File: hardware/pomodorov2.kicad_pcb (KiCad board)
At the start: 2 copper layers, 56 x 41.4 mm, 26 parts, among them J1 USB_B_Micro, J2 TC2050-IDC, J3 SOICbite, U1 MDBT50Q-1MV2, Y1 32.768kHz, Y1 32MHz, Y2 32.768kHz

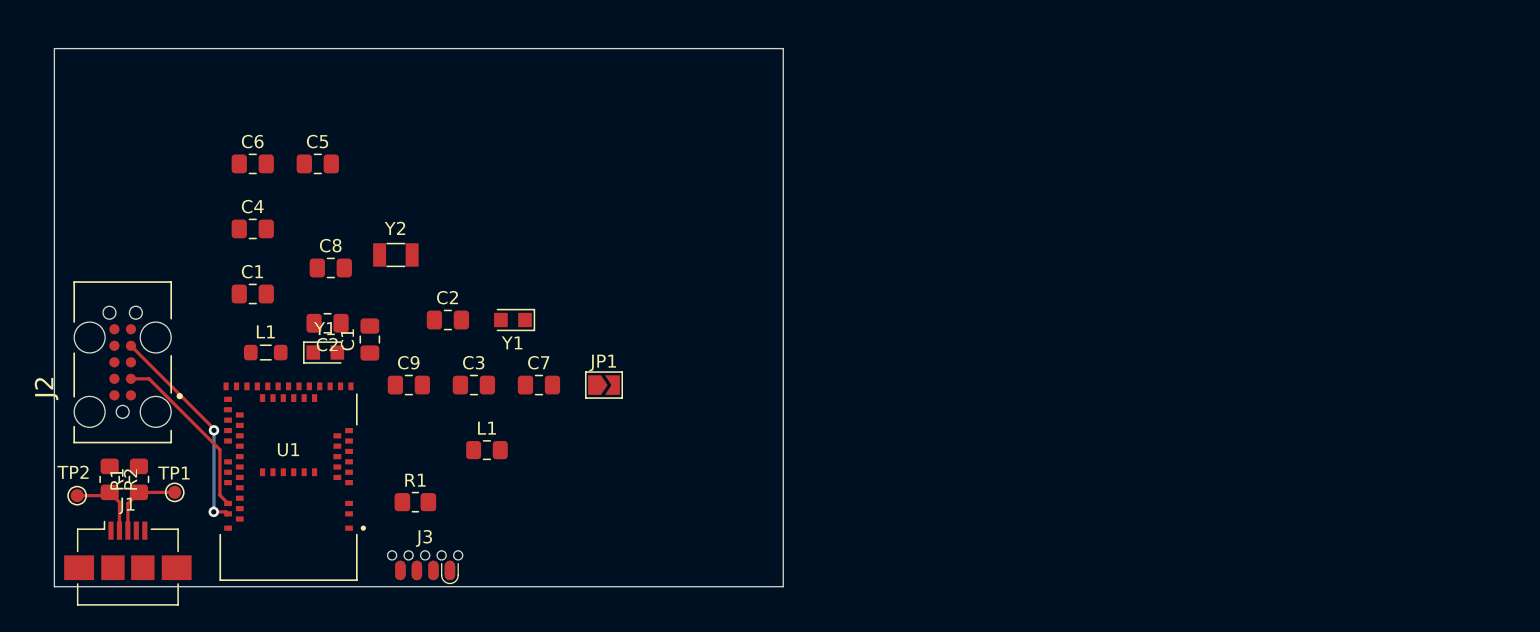
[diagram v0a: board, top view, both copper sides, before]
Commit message: Start on triangular layout
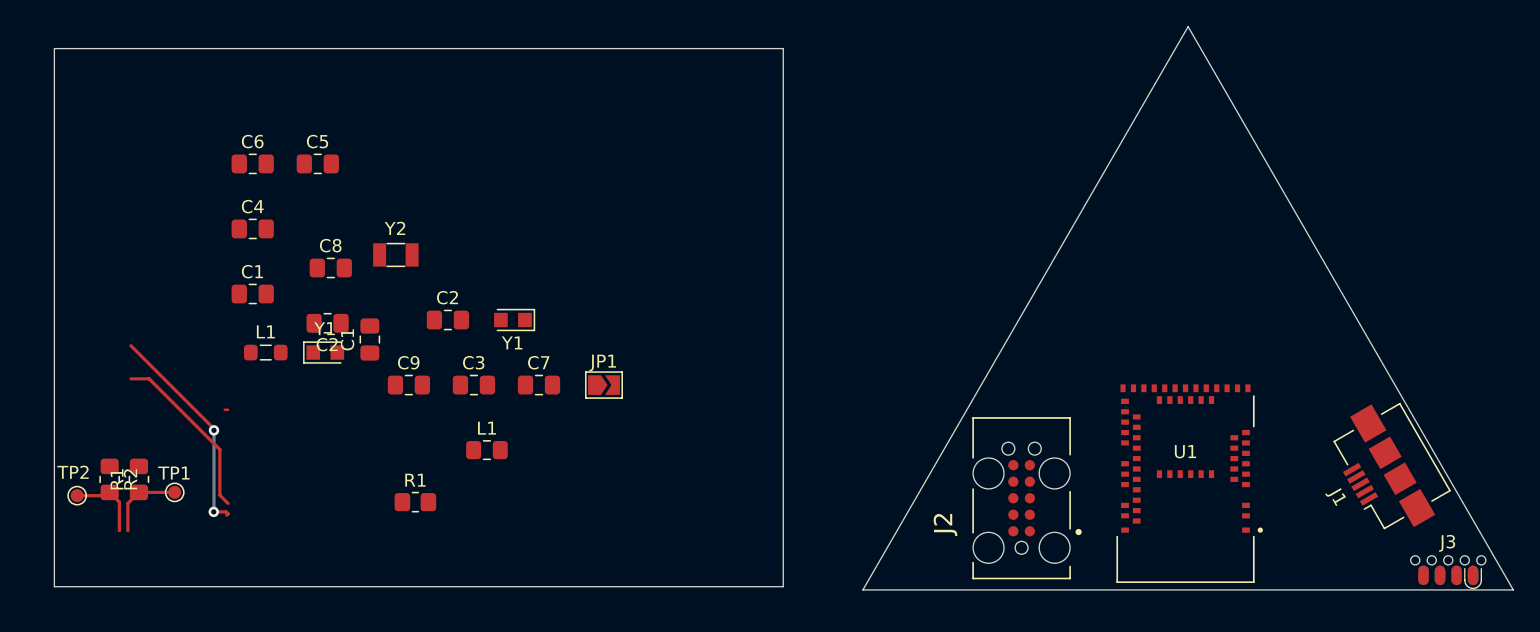
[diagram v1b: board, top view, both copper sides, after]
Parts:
- moved J1 96.3 mm to (190.5, 104.9), turned to 120 degrees
- moved J3 78.7 mm to (195.9, 113.4)
- moved J2 69.9 mm to (163.1, 106.7)
- moved U1 69.0 mm to (175.7, 105.4)
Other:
- board size 56 x 41.4 mm -> 112.2 x 43.3 mm
